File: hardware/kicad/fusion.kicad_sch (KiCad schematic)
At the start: 32 parts, among them J1 BATTERY, J2 LSM6DSOX, J3 PICKIT, J4 HC-05, J5 FLEX, J7 FTDI, SW1 BUTTON, SW2 POWER, SW3 UART, U1 MCP1603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

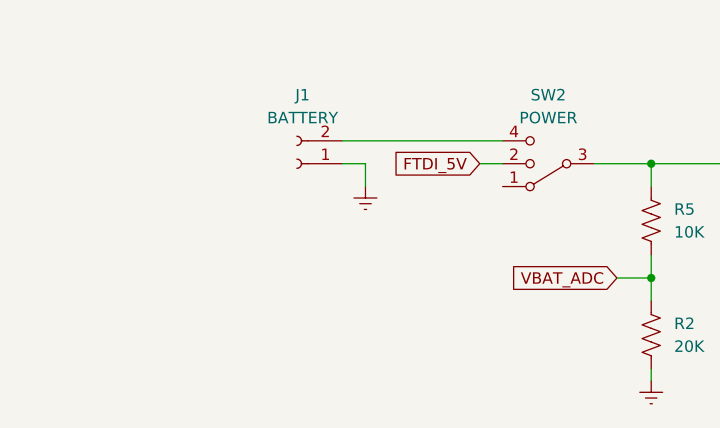
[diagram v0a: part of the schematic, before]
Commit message: 0603 footprints and SP3T
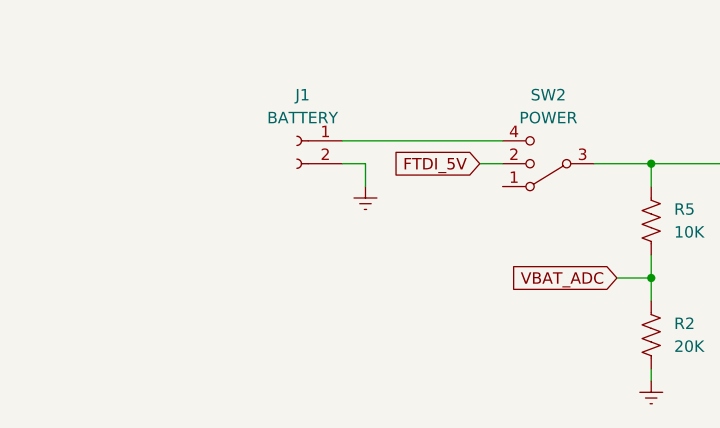
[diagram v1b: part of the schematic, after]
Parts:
- C1, C2, C3, C4, C5, C6, C7, C8: footprint (none) -> Capacitor_SMD:C_0603_1608Metric_Pad1.08x0.95mm_HandSolder
- D1, D2: footprint (none) -> LED_SMD:LED_0603_1608Metric_Pad1.05x0.95mm_HandSolder
- J3: footprint Connector_PinHeader_2.54mm:PinHeader_1x05_P2.54mm_Horizontal -> Connector_PinSocket_2.54mm:PinSocket_1x05_P2.54mm_Vertical
- J7: footprint Connector_PinHeader_2.54mm:PinHeader_1x06_P2.54mm_Horizontal -> Connector_PinSocket_2.54mm:PinSocket_1x06_P2.54mm_Vertical
- L1: footprint (none) -> Inductor_SMD:L_0603_1608Metric_Pad1.05x0.95mm_HandSolder
- R1, R10, R2, R3, R4, R5, R6, R7, R8, R9: footprint (none) -> Resistor_SMD:R_0603_1608Metric_Pad0.98x0.95mm_HandSolder
- SW2: footprint (none) -> Button_Switch_SMD:SW_SP3T_PCM13
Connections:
- net GNDREF: now also J1.2 (Pin_2); no longer J1.1 (Pin_1)
- net at SW2.4: now also J1.1 (Pin_1); no longer J1.2 (Pin_2)
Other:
- moved on the sheet: J1

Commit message: Placing components
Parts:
- removed J5: FLEX, Connector_PinHeader_2.54mm:PinHeader_2x05_P2.54mm_Horizontal, symbol Connector_Generic:Conn_02x05_Counter_Clockwise
- added J5: FLEX, Connector_PinHeader_2.54mm:PinHeader_2x05_P2.54mm_Horizontal, symbol Connector_Generic:Conn_02x05_Odd_Even
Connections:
- net GNDREF: now also J5.10 (Pin_10), J5.2 (Pin_2), J5.4 (Pin_4), J5.6 (Pin_6), J5.8 (Pin_8)
- net INDEX: now also J5.3 (Pin_3)
- net MIDDLE: now also J5.5 (Pin_5)
- net PINKY: now also J5.9 (Pin_9)
- net RING: now also J5.7 (Pin_7)
- net THUMB: now also J5.1 (Pin_1)
- no-connect marks 2 -> 3

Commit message: Route board
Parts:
- removed J4: HC-05, Connector_PinHeader_2.54mm:PinHeader_1x05_P2.54mm_Horizontal, symbol Connector:Conn_01x05_Male
- added J4: HC-05, Connector_PinHeader_2.54mm:PinHeader_1x04_P2.54mm_Horizontal, symbol Connector:Conn_01x04_Male
- SW2: footprint Button_Switch_SMD:SW_SP3T_PCM13 -> Fusion:SP3T
- SW3: footprint Button_Switch_THT:SW_CuK_JS202011CQN_DPDT_Straight -> Fusion:SPDT
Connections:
- net BT_KEY is gone; now on net LED: U2.2 (T1CKI/OSC1/CLKIN/RA5)
- net +3V3: now also J4.1 (Pin_1)
- net BT_RX: now also J4.4 (Pin_4)
- net BT_TX: now also J4.3 (Pin_3)
- net GNDREF: now also J4.2 (Pin_2)
- net LED: no longer U2.6 (RC4/C2OUT/P1B)
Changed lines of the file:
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@@
+    (stroke (width 0) (type default) (color 0 0 0 0))
+  )
+  (wire (pts (xy 172.72 114.3) (xy 176.53 114.3))
     (stroke (width 0) (type default) (color 0 0 0 0))
   )
@@
     (stroke (width 0) (type default) (color 0 0 0 0))
   )
-  (wire (pts (xy 92.71 111.76) (xy 96.52 111.76))
-    (stroke (width 0) (type default) (color 0 0 0 0))
-  )
   (wire (pts (xy 26.67 166.37) (xy 29.21 166.37))
     (stroke (width 0) (type default) (color 0 0 0 0))
@@
     (stroke (width 0) (type default) (color 0 0 0 0))
   )
-  (wire (pts (xy 207.01 78.74) (xy 212.09 78.74))
-    (stroke (width 0) (type default) (color 0 0 0 0))
-  )
   (wire (pts (xy 90.17 177.8) (xy 90.17 180.34))
     (stroke (width 0) (type default) (color 0 0 0 0))
@@
   )
   (wire (pts (xy 49.53 161.29) (xy 49.53 172.72))
-    (stroke (width 0) (type default) (color 0 0 0 0))
-  )
-  (wire (pts (xy 172.72 114.3) (xy 176.53 114.3))
     (stroke (width 0) (type default) (color 0 0 0 0))
   )
@@
     )
   )
-  (global_label "BT_KEY" (shape input) (at 207.01 78.74 180) (fields_autoplaced)
-    (effects (font (size 1.27 1.27)) (justify right))
-    (property "Intersheet References" "${INTERSHEET_REFS}" (id 0) (at 197.884 78.6606 0)
-      (effects (font (size 1.27 1.27)) (justify right) hide)
-    )
-  )
   (global_label "FTDI_RX" (shape input) (at 248.92 76.2 180) (fields_autoplaced)
     (effects (font (size 1.27 1.27)) (justify right))
@@
     )
   )
+  (global_label "LED" (shape input) (at 176.53 114.3 0) (fields_autoplaced)
+    (effects (font (size 1.27 1.27)) (justify left))
+    (property "Intersheet References" "${INTERSHEET_REFS}" (id 0) (at 182.3902 114.3794 0)
+      (effects (font (size 1.27 1.27)) (justify left) hide)
+    )
+  )
   (global_label "MOSI" (shape input) (at 207.01 41.91 180) (fields_autoplaced)
     (effects (font (size 1.27 1.27)) (justify right))
@@
     )
   )
-  (global_label "LED" (shape input) (at 92.71 111.76 180) (fields_autoplaced)
-    (effects (font (size 1.27 1.27)) (justify right))
-    (property "Intersheet References" "${INTERSHEET_REFS}" (id 0) (at 86.8498 111.6806 0)
-      (effects (font (size 1.27 1.27)) (justify right) hide)
-    )
-  )
   (global_label "TX" (shape input) (at 227.33 114.3 180) (fields_autoplaced)
     (effects (font (size 1.27 1.27)) (justify right))
@@
     (property "Intersheet References" "${INTERSHEET_REFS}" (id 0) (at 239.3102 71.0406 0)
       (effects (font (size 1.27 1.27)) (justify right) hide)
-    )
-  )
-  (global_label "BT_KEY" (shape input) (at 176.53 114.3 0) (fields_autoplaced)
-    (effects (font (size 1.27 1.27)) (justify left))
-    (property "Intersheet References" "${INTERSHEET_REFS}" (id 0) (at 185.656 114.2206 0)
-      (effects (font (size 1.27 1.27)) (justify left) hide)
     )
   )
@@
     (pin "6")
   )
-  (symbol (lib_id "Connector:Conn_01x05_Male") (at 217.17 73.66 180) (unit 1)
-    (in_bom yes) (on_board yes)
-    (property "Reference" "J4" (id 0) (at 218.44 72.39 0)
-      (effects (font (size 1.27 1.27)) (justify right))
-    )
-    (property "Value" "HC-05" (id 1) (at 218.44 74.9299 0)
-      (effects (font (size 1.27 1.27)) (justify right))
-    )
-    (property "Footprint" "Connector_PinHeader_2.54mm:PinHeader_1x05_P2.54mm_Horizontal" (id 2) (at 217.17 73.66 0)
-      (effects (font (size 1.27 1.27)) hide)
-    )
-    (property "Datasheet" "~" (id 3) (at 217.17 73.66 0)
-      (effects (font (size 1.27 1.27)) hide)
-    )
-    (pin "1")
-    (pin "2")
-    (pin "3")
-    (pin "4")
-    (pin "5")
-  )
   (symbol (lib_id "Connector:Conn_01x05_Male") (at 259.08 41.91 180) (unit 1)
     (in_bom yes) (on_board yes)
@@
     (property "Reference" "SW3" (id 0) (at 234.95 106.68 0))
     (property "Value" "UART" (id 1) (at 234.95 109.22 0))
-    (property "Footprint" "Button_Switch_THT:SW_CuK_JS202011CQN_DPDT_Straight" (id 2) (at 234.95 114.3 0)
+    (property "Footprint" "Fusion:SPDT" (id 2) (at 234.95 114.3 0)
       (effects (font (size 1.27 1.27)) hide)
     )
@@
     (property "Reference" "SW3" (id 0) (at 234.95 90.17 0))
     (property "Value" "UART" (id 1) (at 234.95 92.71 0))
-    (property "Footprint" "Button_Switch_THT:SW_CuK_JS202011CQN_DPDT_Straight" (id 2) (at 234.95 97.79 0)
+    (property "Footprint" "Fusion:SPDT" (id 2) (at 234.95 97.79 0)
       (effects (font (size 1.27 1.27)) hide)
     )
@@
     (pin "1")
   )
+  (symbol (lib_id "Connector:Conn_01x04_Male") (at 217.17 73.66 180) (unit 1)
+    (in_bom yes) (on_board yes) (fields_autoplaced)
+    (property "Reference" "J4" (id 0) (at 218.44 71.1199 0)
+      (effects (font (size 1.27 1.27)) (justify right))
+    )
+    (property "Value" "HC-05" (id 1) (at 218.44 73.6599 0)
+      (effects (font (size 1.27 1.27)) (justify right))
+    )
+    (property "Footprint" "Connector_PinHeader_2.54mm:PinHeader_1x04_P2.54mm_Horizontal" (id 2) (at 217.17 73.66 0)
+      (effects (font (size 1.27 1.27)) hide)
+    )
+    (property "Datasheet" "~" (id 3) (at 217.17 73.66 0)
+      (effects (font (size 1.27 1.27)) hide)
+    )
+    (pin "1")
+    (pin "2")
+    (pin "3")
+    (pin "4")
+  )
   (symbol (lib_id "power:GNDREF") (at 62.23 40.64 0) (unit 1)
     (in_bom yes) (on_board yes) (fields_autoplaced)
@@
     (property "Reference" "SW2" (id 0) (at 82.55 30.48 0))
     (property "Value" "POWER" (id 1) (at 82.55 33.02 0))
-    (property "Footprint" "Button_Switch_SMD:SW_SP3T_PCM13" (id 2) (at 98.425 42.545 0)
+    (property "Footprint" "Fusion:SP3T" (id 2) (at 98.425 42.545 0)
       (effects (font (size 1.27 1.27)) hide)
     )
@@
       (reference "J3") (unit 1) (value "PICKIT") (footprint "Connector_PinSocket_2.54mm:PinSocket_1x05_P2.54mm_Vertical")
     )
-    (path "/1489d60f-98c9-4dde-bc1c-e357d13159f0"
-      (reference "J4") (unit 1) (value "HC-05") (footprint "Connector_PinHeader_2.54mm:PinHeader_1x05_P2.54mm_Horizontal")
+    (path "/9d0a4cb0-b9ef-4f0e-8fc8-06d04a746603"
+      (reference "J4") (unit 1) (value "HC-05") (footprint "Connector_PinHeader_2.54mm:PinHeader_1x04_P2.54mm_Horizontal")
     )
     (path "/782e7ab6-d607-4e67-a926-392d32564367"
@@
     )
     (path "/d86cd546-387f-43ce-987b-67139a87e556"
-      (reference "SW2") (unit 1) (value "POWER") (footprint "Button_Switch_SMD:SW_SP3T_PCM13")
+      (reference "SW2") (unit 1) (value "POWER") (footprint "Fusion:SP3T")
     )
     (path "/6b53fed9-c9c4-473c-8af9-9f63c05e1633"
-      (reference "SW3") (unit 1) (value "UART") (footprint "Button_Switch_THT:SW_CuK_JS202011CQN_DPDT_Straight")
+      (reference "SW3") (unit 1) (value "UART") (footprint "Fusion:SPDT")
     )
     (path "/23868c91-5ed1-4fde-9299-051e4d98eab8"
-      (reference "SW3") (unit 2) (value "UART") (footprint "Button_Switch_THT:SW_CuK_JS202011CQN_DPDT_Straight")
+      (reference "SW3") (unit 2) (value "UART") (footprint "Fusion:SPDT")
     )
     (path "/4097a3ad-7c35-487b-a832-47992aa626df"

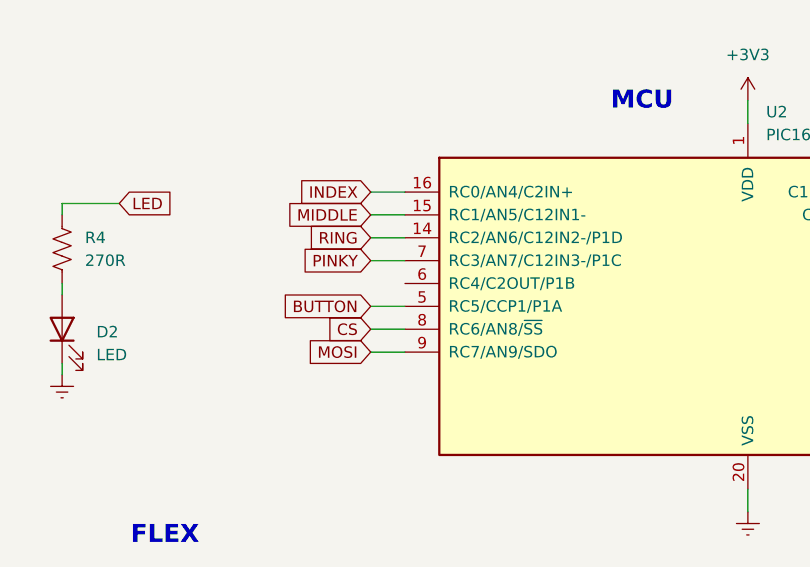
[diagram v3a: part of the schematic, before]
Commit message: Rounded corners, mounting holes, and DRC
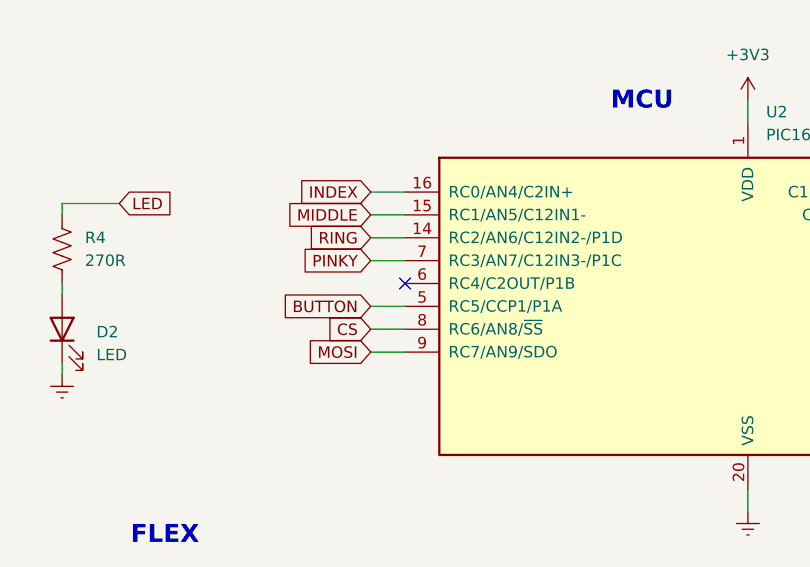
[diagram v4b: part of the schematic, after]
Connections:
- no-connect marks 3 -> 4
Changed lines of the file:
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@@
   (no_connect (at 254 68.58))
   (no_connect (at 254 78.74))
+  (no_connect (at 96.52 111.76))
   (wire (pts (xy 41.91 171.45) (xy 90.17 171.45))
     (stroke (width 0) (type default) (color 0 0 0 0))
